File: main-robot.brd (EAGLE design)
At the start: 100 x 100 mm, 13 parts, among them U1 TEENSY_3.5_DIL

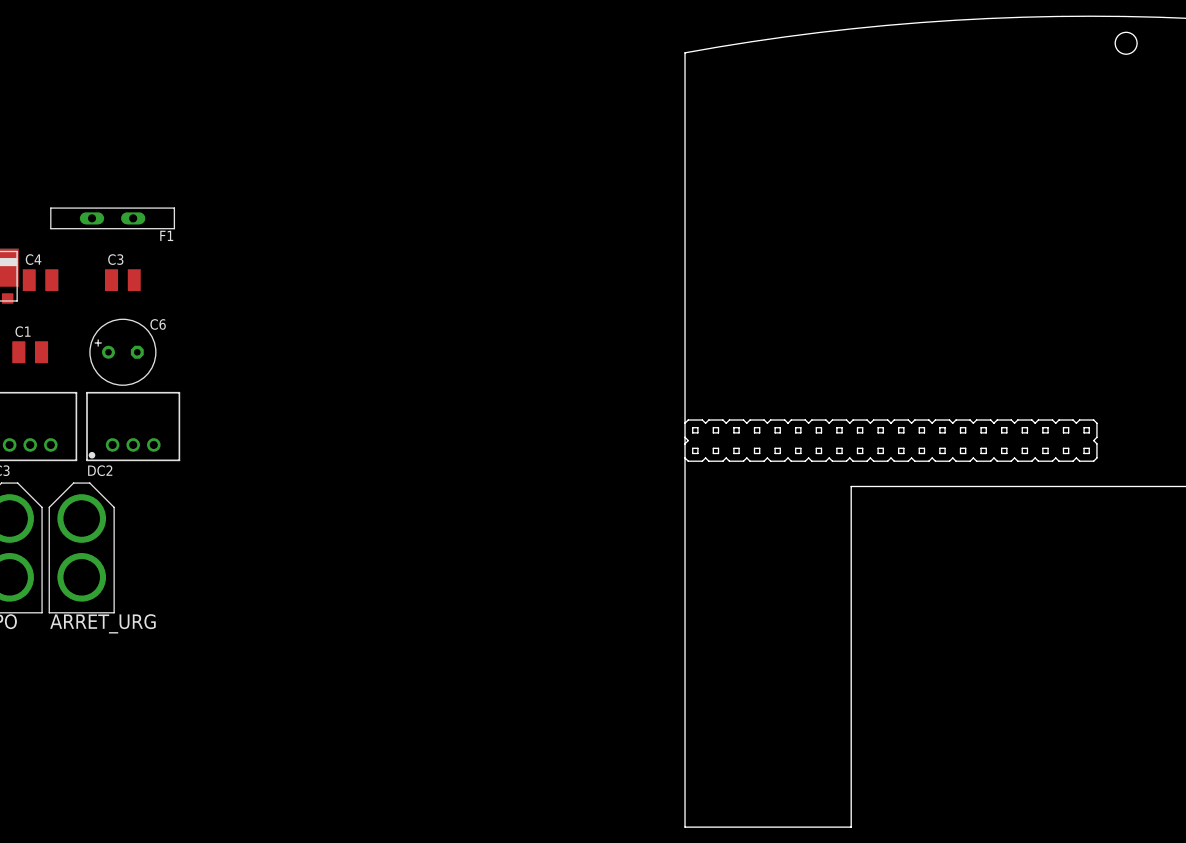
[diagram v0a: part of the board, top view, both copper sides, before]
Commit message: brd: rpi placement
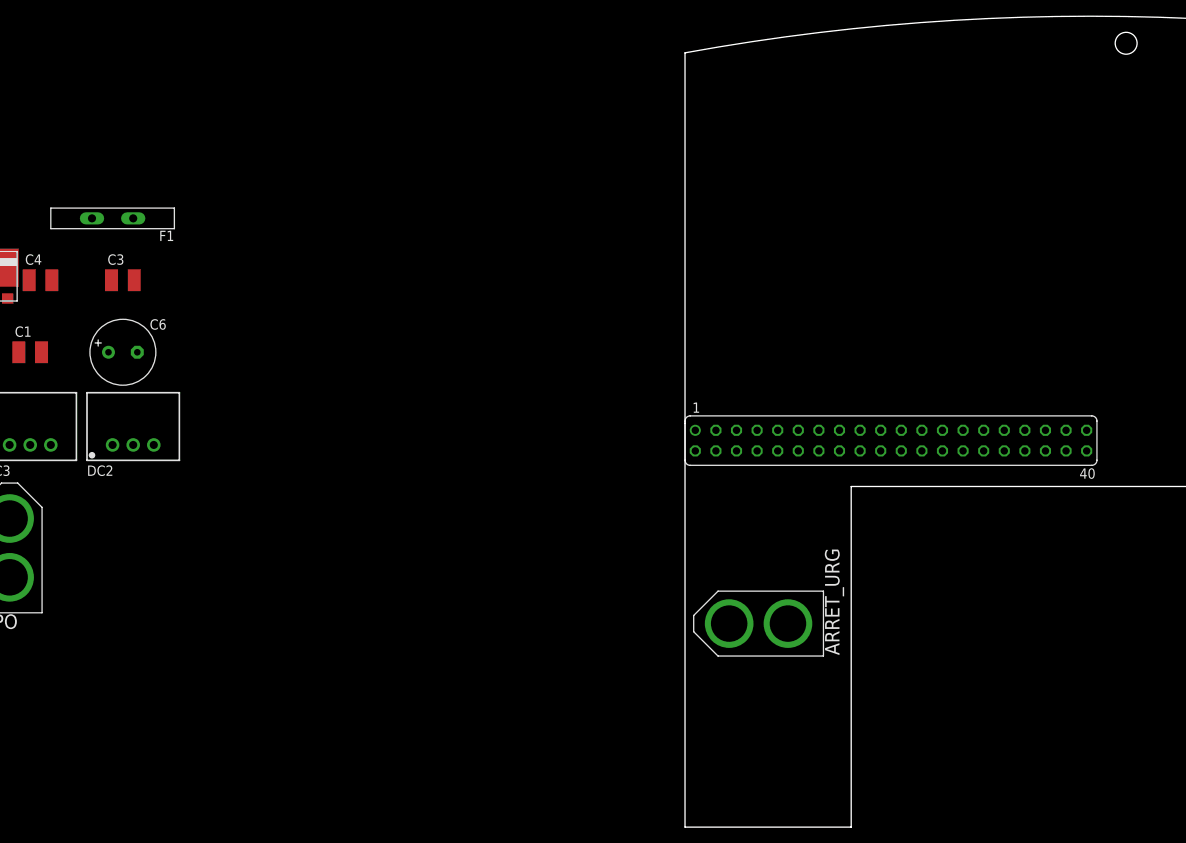
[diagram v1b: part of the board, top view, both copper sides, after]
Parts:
- added SV1: (no value), con-lsta:FE20-2
- moved ARRET_URG 84.0 mm to (9.07, 25.1), turned to 90 degrees
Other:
- outline, holes or cut-outs redrawn

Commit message: progess in schematic
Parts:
- removed ARRET_URG, LIPO: XT-60, con-xt:XT-60
- added AR-URG-1, AR-URG-2, LIPO+, LIPO-: TPPAD1-20Y, testpad:P1-20Y
- added C10, C8: 100nF, resistor:C0805
- added C7: 10nF, resistor:C0805
- added C9: 270µF, resistor:E3,5-8
- added CON1, CON2: AX12, con-molex-dynamixel:5267-03A
- added CON3: GENERIC-3PIN53253, con-molex-dynamixel:53253-0370
- added DISPLAY, ENC_D, ENC_G: JST-04TOP, con-jst-gh:BM04B-GHS
- added EXT_1: JST-06SIDE, con-jst-gh:SM06B-GHS
- added EXT_2: JST-06TOP, con-jst-gh:BM06B-GHS
- added JUMPER: JST-02SIDE, con-jst-gh:SM02B-GHS
- added LEVEL_SHIFTER1:Q1: BSS138, transistor-small-signal:SOT23
- added LEVEL_SHIFTER1:R1, LEVEL_SHIFTER1:R2, R5, R7: 10k, resistor:R0805
- added MOTOR: (no value), pinhead:1X06
- added R1, R2, R3, R4, R8: 1k, resistor:R0805
- added R6: 820, resistor:R0805
- added TOF_AR: JST-03SIDE, con-jst-gh:SM03B-GHS
- added TOF_ARD, TOF_ARG, TOF_AV: JST-03TOP, con-jst-gh:BM03B-GHS
- added U2: VNH7100AS, h-bridge:SOIC127P600X175-16M
- C1, C2, C3, C4: value 10µF/50V -> 10µF
- C5, C6: value 220µF/25V -> 220µF
- DC2: device dc-dc-converter:SIP3 -> traco-power:TSR1
- DC3: device dc-dc-converter:SIP3 -> traco-power:TSR2
- moved C5 132.5 mm to (36.0, 69.0)
- moved DC3 132.5 mm to (51.0, 61.0)
- moved DC2 121.8 mm to (51.0, 73.0)
- moved C6 108.5 mm to (37.0, 80.0)
- moved C4 108.4 mm to (27.0, 88.0)
- moved C3 108.3 mm to (37.0, 88.0)
- moved C2 108.1 mm to (15.0, 80.0)
- moved C1 107.9 mm to (25.0, 80.0)
- moved D1 98.5 mm to (3.00, 21.0)
- moved F1 95.9 mm to (1.70, 12.0), flipped to the bottom, turned to 270 degrees
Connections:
- removed net 3.3V: U1.3.3V, U1.3.3V3
- removed net AGND: U1.AGND
- removed net VIN: U1.VIN
- new net +12V: AR-URG-2.TP, C3.1, C4.1, C8.1, C9.+, CON1.2, CON2.2, DC2.1, EXT_1.5, EXT_2.5, U2.12, U2.4, U2.5
- new net +5V/1: C6.+, DC2.3, DISPLAY.4, ENC_D.4, ENC_G.4, MOTOR.4, U1.VIN
- new net +5V/2: C5.+, DC3.3, SV1.2, SV1.4
- new net 3V3: EXT_1.4, EXT_2.4, R7.1, TOF_AR.2, TOF_ARD.2, TOF_ARG.2, TOF_AV.2, U1.3.3V, U1.3.3V3
- new net AX12_DATA: CON1.1, CON2.1, EXT_1.2, EXT_2.2
- new net ENC_D_A: ENC_D.2
- new net ENC_D_B: ENC_D.1
- new net ENC_G_A: ENC_G.2
- new net ENC_G_B: ENC_G.1
- new net ENC_MOT_A: MOTOR.5
- new net ENC_MOT_B: MOTOR.6
- new net JUMPER: R8.1
- new net LEVEL_SHIFTER1:HV: LEVEL_SHIFTER1:R2.1
- new net LEVEL_SHIFTER1:IO_HV: LEVEL_SHIFTER1:Q1.3, LEVEL_SHIFTER1:R2.2
- new net LEVEL_SHIFTER1:IO_LV: LEVEL_SHIFTER1:Q1.2, LEVEL_SHIFTER1:R1.2
- new net LEVEL_SHIFTER1:LV: LEVEL_SHIFTER1:Q1.1, LEVEL_SHIFTER1:R1.1
- new net MOT_CS: C7.2, R5.1
- new net MOT_INA: R1.1
- new net MOT_INB: R2.1
- new net MOT_PWM: R3.1
- new net MOT_SEL: R4.1
- new net N$10: C10.2, JUMPER.1, R7.2, R8.2
- new net N$14: EXT_1.1
- new net N$15: EXT_2.1
- new net N$4: MOTOR.2, U2.10, U2.7
- new net N$5: R3.2, U2.11
- new net N$6: R2.2, U2.6
- new net N$7: R1.2, U2.3
- new net N$8: R4.2, U2.14
- new net N$9: R5.2, R6.2, U2.13
- new net SCL: DISPLAY.1
- new net SDA: DISPLAY.2
- new net TOF_DATA: EXT_1.3, EXT_2.3, TOF_AR.3, TOF_ARD.3, TOF_ARG.3, TOF_AV.3
- net GND: now also C10.1, C3.2, C4.2, C6.-, C7.1, C8.2, C9.-, CON1.3, CON2.3, DC2.2, DISPLAY.3, ENC_D.3, ENC_G.3, EXT_1.6, EXT_2.6, JUMPER.2, LIPO-.TP, MOTOR.3, R6.1, SV1.14, SV1.20, SV1.25, SV1.30, SV1.34, SV1.39, SV1.6, SV1.9, TOF_AR.1, TOF_ARD.1, TOF_ARG.1, TOF_AV.1, U1.AGND, U2.1, U2.16, U2.8, U2.9; no longer LIPO.(-)
- net N$1: now also AR-URG-1.TP
- net N$3: now also MOTOR.1, U2.15, U2.2; no longer C5.+, DC3.3
- net V_LIPO: now also LIPO+.TP; no longer LIPO.(+)
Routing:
- added copper zone on layer 1, net +12V

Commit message: progress on schematic
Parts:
- removed C2, C3: 10µF, resistor:C1210
- removed C7: 10nF, resistor:C0805
- removed LEVEL_SHIFTER1:Q1: BSS138, transistor-small-signal:SOT23
- removed LEVEL_SHIFTER1:R1, LEVEL_SHIFTER1:R2, R5: 10k, resistor:R0805
- removed R3, R4: 1k, resistor:R0805
- removed R6: 820, resistor:R0805
- removed U2: VNH7100AS, h-bridge:SOIC127P600X175-16M
- added D2: (no value), diode:SMB
- added DC1: TSR 1-2450, traco-power:TSR1
- added F2: MF-LSMF300, polyswitch:MF-LSMF300
- added HB1:C7, HB2:C7: 10nF, resistor:C0805
- added HB1:C8, HB2:C8: 100nF, resistor:C0805
- added HB1:C9, HB2:C9: 220µF, resistor:PANASONIC_D
- added HB1:R1, HB1:R2, HB1:R3, HB1:R4, HB1:R6, HB2:R1, HB2:R2, HB2:R3, HB2:R4, HB2:R6: 1k, resistor:R0805
- added HB1:R10, HB2:R10: 15k, resistor:R0805
- added HB1:R5, HB1:R9, HB2:R5, HB2:R9, S1:R1, S1:R2: 10k, resistor:R0805
- added HB1:U2, HB2:U2: VNH7100AS, h-bridge:SOIC127P600X175-16M
- added JMP1: 0R-JUMPA, jump-0r-smd:A0R-JMP
- added JP1: (no value), pinhead:1X02
- added LED1, LED2, LED3, LED4, LED5, LED6, LED7, LED8: (no value), led:1206
- added LEDS: JST-05SIDE, con-jst-gh:SM05B-GHS
- added S1:Q1: BSS138, transistor-small-signal:SOT23
- added SW1: SWITCH-SPDT-H, switch-rs-pro:SWITCH_SPDT_H
- added SW2, SW3, SW4, SW5, SW6, SW7: PUSH-BUTTON436331045822, push-button:436331045822
- C1, C4: value 10µF -> 22µF; device resistor:C1210 -> resistor:C0805
- C5, C6: device resistor:E3,5-8 -> resistor:PANASONIC_D
- C8: value 100nF -> 22µF
- C9: value 270µF -> 220µF; device resistor:E3,5-8 -> resistor:PANASONIC_D
- CON3: value GENERIC-3PIN53253 -> GENERIC-4PIN53253; device con-molex-dynamixel:53253-0370 -> con-molex-dynamixel:53253-0470
- R1, R2: value 1k -> 10k
- U1: value TEENSY_3.5_DIL -> TEENSY_3.5_DIL+4; device Teensy_libSG:TEENSY_3.5_DIL -> Teensy_libSG:TEENSY_3.5_DIL+4
- moved C10 134.8 mm to (-25.0, 60.0)
- moved R7 134.8 mm to (-25.0, 55.0)
- moved R8 134.8 mm to (-25.0, 50.0)
- moved C9 96.3 mm to (-101.0, -41.0)
- moved C8 92.7 mm to (-102.0, -49.0)
- moved R1 84.7 mm to (-94.0, -14.0)
- moved R2 84.7 mm to (-94.0, -19.0)
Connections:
- net N$14 renamed EXT_DATA
- removed net LEVEL_SHIFTER1:HV: LEVEL_SHIFTER1:R2.1
- removed net LEVEL_SHIFTER1:IO_HV: LEVEL_SHIFTER1:Q1.3, LEVEL_SHIFTER1:R2.2
- removed net LEVEL_SHIFTER1:IO_LV: LEVEL_SHIFTER1:Q1.2, LEVEL_SHIFTER1:R1.2
- removed net LEVEL_SHIFTER1:LV: LEVEL_SHIFTER1:Q1.1, LEVEL_SHIFTER1:R1.1
- removed net N$9: R5.2, R6.2, U2.13
- new net AREF: U1.AREF
- new net EXT_+5V: C9.+, DC1.3, HB2:C8.1, HB2:C9.+, HB2:U2.12, HB2:U2.4, HB2:U2.5, JMP1.1
- new net EXT_VCC: EXT_2.1, JMP1.2
- new net FLAG_CS: HB2:R10.2, HB2:R9.1
- new net FLAG_GPIO1: R1.1
- new net FLAG_GPIO2: R2.1
- new net FLAG_INA: HB2:R1.1
- new net FLAG_INB: HB2:R2.1
- new net FLAG_PWM: HB2:R3.1
- new net FLAG_SEL: HB2:R4.1
- new net HB1:N$13: HB1:C7.2, HB1:R5.1, HB1:R9.2
- new net HB1:N$5: HB1:R3.2, HB1:U2.11
- new net HB1:N$6: HB1:R2.2, HB1:U2.6
- new net HB1:N$7: HB1:R1.2, HB1:U2.3
- new net HB1:N$8: HB1:R4.2, HB1:U2.14
- new net HB1:N$9: HB1:R5.2, HB1:R6.2, HB1:U2.13
- new net HB2:N$13: HB2:C7.2, HB2:R5.1, HB2:R9.2
- new net HB2:N$5: HB2:R3.2, HB2:U2.11
- new net HB2:N$6: HB2:R2.2, HB2:U2.6
- new net HB2:N$7: HB2:R1.2, HB2:U2.3
- new net HB2:N$8: HB2:R4.2, HB2:U2.14
- new net HB2:N$9: HB2:R5.2, HB2:R6.2, HB2:U2.13
- new net LED_DATA: LEDS.5
- new net N$11: AR-URG-1.TP, D1.-, SW1.C
- new net N$12: D2.A, JP1.2
- new net S1:HV: S1:R2.1
- new net S1:IO_HV: S1:Q1.3, S1:R2.2
- new net S1:IO_LV: S1:Q1.2, S1:R1.2
- new net S1:LV: S1:Q1.1, S1:R1.1
- new net VUSB: JP1.1, U1.VUSB
- net +12V: now also DC1.1, F2.1, HB1:C8.1, HB1:C9.+, HB1:U2.12, HB1:U2.4, HB1:U2.5; no longer C3.1, C9.+, U2.12, U2.4, U2.5
- net +5V/1: now also D2.C, LEDS.3, LEDS.4
- net GND: now also DC1.2, HB1:C7.1, HB1:C8.2, HB1:C9.-, HB1:R10.1, HB1:R6.1, HB1:U2.1, HB1:U2.16, HB1:U2.8, HB1:U2.9, HB2:C7.1, HB2:C8.2, HB2:C9.-, HB2:R10.1, HB2:R6.1, HB2:U2.1, HB2:U2.16, HB2:U2.8, HB2:U2.9, LEDS.1, LEDS.2, SW1.CASE1, SW1.CASE2; no longer C2.2, C3.2, C7.1, R6.1, U2.1, U2.16, U2.8, U2.9
- net MOT_CS: now also HB1:R10.2, HB1:R9.1; no longer C7.2, R5.1
- net MOT_INA: now also HB1:R1.1; no longer R1.1
- net MOT_INB: now also HB1:R2.1; no longer R2.1
- net MOT_PWM: now also HB1:R3.1; no longer R3.1
- net MOT_SEL: now also HB1:R4.1; no longer R4.1
- net N$1: now also SW1.2; no longer AR-URG-1.TP, C2.1, D1.-
- net N$15: now also F2.2, JMP1.3; no longer EXT_2.1
- net N$3: now also HB1:U2.15, HB1:U2.2; no longer U2.15, U2.2
- net N$4: now also HB1:U2.10, HB1:U2.7; no longer U2.10, U2.7
- net N$5: now also CON3.1, HB2:U2.15, HB2:U2.2; no longer R3.2, U2.11
- net N$6: now also CON3.2, HB2:U2.10, HB2:U2.7; no longer R2.2, U2.6
- net N$7: now also CON3.3; no longer U2.3
- net N$8: now also CON3.4, R2.2; no longer R4.2, U2.14

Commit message: v1 schematics
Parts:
- removed CON3: GENERIC-4PIN53253, con-molex-dynamixel:53253-0470
- added FLAG: GENERIC-4PIN53253, con-molex-dynamixel:53253-0470
- added R10, R12, R14, R16, R4, R6, S2:R1, S2:R2, S3:R1, S3:R2, S4:R1, S4:R2, S5:R1, S5:R2: 10k, resistor:R0805
- added R11, R13, R15, R17, R18, R3, R5, R9: 470, resistor:R0805
- added RTC1: RTC, rtc-raspberry-pi:RTC
- added S2:Q1, S3:Q1, S4:Q1, S5:Q1: BSS138, transistor-small-signal:SOT23
- D2: value (none) -> SS56B
- JP1: value (none) -> VUSB
- SV1: value (none) -> RPI
- SW3, SW4: value PUSH-BUTTON436331045822 -> PUSH-BUTTON; device push-button:436331045822 -> push-button:PUSH-BUTTON
- U1: device Teensy_libSG:TEENSY_3.5_DIL+4 -> teensy:TEENSY_3.5_DIL+4
- moved LED7 252.5 mm to (-113.0, -248.0)
- moved SW7 221.8 mm to (47.7, 98.0)
- moved LED8 164.4 mm to (-113.0, -231.0)
- moved LED4 149.9 mm to (-113.0, -130.0)
- moved LED3 137.9 mm to (-113.0, -113.0)
- moved SW6 133.7 mm to (40.5, 97.9), turned to 2 degrees
- moved LED2 126.3 mm to (-115.0, -96.0)
- moved SW5 111.9 mm to (33.2, 97.5), turned to 3.5 degrees
- moved SW4 99.7 mm to (40.0, 85.0)
- moved SW3 74.1 mm to (28.0, 85.0), turned to 180 degrees
- moved SW2 54.5 mm to (25.8, 97.0), turned to 5.5 degrees
- moved C4 17.0 mm to (28.0, 71.0)
- moved C6 12.2 mm to (35.0, 68.0)
- moved C1 11.4 mm to (28.0, 69.0)
- moved LED5 10.0 mm to (-97.0, 4.00)
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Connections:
- removed net S1:HV: S1:R2.1
- removed net S1:IO_HV: S1:Q1.3, S1:R2.2
- removed net S1:IO_LV: S1:Q1.2, S1:R1.2
- removed net S1:LV: S1:Q1.1, S1:R1.1
- new net AX12_DATA_LV: S1:Q1.2, S1:R1.2, U1.10, U1.9
- new net EXT_DATA_LV: S2:Q1.2, S2:R1.2, U1.7, U1.8
- new net IN_COLOR_A: R16.1, SW7.2, SW7.4, U1.25
- new net IN_COLOR_B: R14.1, SW6.2, SW6.4, U1.26
- new net IN_JUMPER: C10.2, R7.2, R8.2, U1.6
- new net LED_COLOR_A: R15.2, U1.35/A16
- new net LED_COLOR_B: R13.2, U1.36/A17
- new net LED_DATA_LV: S5:Q1.2, S5:R1.2, U1.24
- new net LED_DEBUG_A: R17.2, U1.37/A18
- new net LED_DEBUG_B: R18.2, U1.38/A19
- new net N$13: RTC1.SDA, SV1.3
- new net N$14: RTC1.SCL, SV1.5
- new net N$16: LED2.A, R5.1
- new net N$17: LED3.A, R9.1
- new net N$18: LED4.A, R11.1
- new net N$19: LED7.A, R15.1
- new net N$20: LED5.A, R18.1
- new net N$21: LED6.A, R17.1
- new net N$9: LED1.A, R3.1
- new net RPI_3V3: R10.2, R12.2, R4.2, R6.2, RTC1.VIN, SV1.1
- new net RPI_IN_MATCH: R12.1, SV1.37, SW5.2, SW5.4
- new net RPI_IN_NET1: R6.1, SV1.11, SW3.3, SW3.4
- new net RPI_IN_NET2: R10.1, SV1.15, SW4.3, SW4.4
- new net RPI_IN_PWDN: R4.1, SV1.29, SW2.2, SW2.4
- new net RPI_LED_MATCH: R11.2, SV1.33
- new net RPI_LED_NET1: R5.2, SV1.13
- new net RPI_LED_NET2: R9.2, SV1.16
- new net RPI_LED_PWR: R3.2, SV1.31
- new net SCL_LV: S4:Q1.2, S4:R1.2, U1.19/A5
- new net SDA_LV: S3:Q1.2, S3:R1.2, U1.18/A4
- net +5V/1: now also S1:R2.1, S2:R2.1, S3:R2.1, S4:R2.1, S5:R2.1
- net 3V3: now also R14.2, R16.2, S1:Q1.1, S1:R1.1, S2:Q1.1, S2:R1.1, S3:Q1.1, S3:R1.1, S4:Q1.1, S4:R1.1, S5:Q1.1, S5:R1.1
- net AX12_DATA: now also S1:Q1.3, S1:R2.2
- net ENC_D_A: now also U1.11
- net ENC_D_B: now also U1.12
- net ENC_G_A: now also U1.34/A15
- net ENC_G_B: now also U1.33/A14
- net ENC_MOT_A: now also U1.14/A0
- net ENC_MOT_B: now also U1.15/A1
- net EXT_DATA: now also S2:Q1.3, S2:R2.2
- net FLAG_CS: now also U1.16/A2
- net FLAG_GPIO1: now also U1.31/A12
- net FLAG_GPIO2: now also U1.32/A13
- net FLAG_INA: now also U1.23/A9
- net FLAG_INB: now also U1.22/A8
- net FLAG_PWM: now also U1.21/A7
- net FLAG_SEL: now also U1.20/A6
- net GND: now also LED1.C, LED2.C, LED3.C, LED4.C, LED5.C, LED6.C, LED7.C, LED8.C, RTC1.GND, SW2.1, SW2.3, SW3.1, SW3.2, SW4.1, SW4.2, SW5.1, SW5.3, SW6.1, SW6.3, SW7.1, SW7.3
- net JUMPER: now also JUMPER.1
- net LED_DATA: now also S5:Q1.3, S5:R2.2
- net MOT_CS: now also U1.17/A3
- net MOT_INA: now also U1.2
- net MOT_INB: now also U1.3
- net MOT_PWM: now also U1.4
- net MOT_SEL: now also U1.5
- net N$10: now also LED8.A, R13.1; no longer C10.2, JUMPER.1, R7.2, R8.2
- net N$5: now also FLAG.1; no longer CON3.1
- net N$6: now also FLAG.2; no longer CON3.2
- net N$7: now also FLAG.3; no longer CON3.3
- net N$8: now also FLAG.4; no longer CON3.4
- net SCL: now also S4:Q1.3, S4:R2.2
- net SDA: now also S3:Q1.3, S3:R2.2
- net TOF_DATA: now also U1.0, U1.1

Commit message: brd: components placement
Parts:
- moved R15 382.8 mm to (47.0, 94.0), flipped to the bottom, turned to 180 degrees
- moved LED7 378.8 mm to (47.7, 95.0)
- moved R13 364.5 mm to (40.0, 94.0), flipped to the bottom, turned to 180 degrees
- moved R18 361.4 mm to (96.0, 24.0)
- moved LED8 360.3 mm to (40.6, 94.9), turned to 2 degrees
- moved R17 354.4 mm to (96.0, 22.0)
- moved R16 344.6 mm to (86.0, 29.0)
- moved S5:R2 331.1 mm to (80.0, 46.0), flipped to the bottom, turned to 270 degrees
- moved R14 329.5 mm to (86.0, 27.0)
- moved S5:R1 324.4 mm to (78.0, 46.0), flipped to the bottom, turned to 270 degrees
- moved S4:R2 318.7 mm to (80.0, 51.0), flipped to the bottom, turned to 270 degrees
- moved S5:Q1 315.6 mm to (75.0, 45.0), flipped to the bottom, turned to 270 degrees
- moved S4:R1 312.1 mm to (78.0, 51.0), flipped to the bottom, turned to 270 degrees
- moved S4:Q1 303.4 mm to (75.0, 50.0), flipped to the bottom, turned to 270 degrees
- moved S3:R2 291.8 mm to (69.0, 46.0), flipped to the bottom, turned to 270 degrees
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
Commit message: brd: begin routing
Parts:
- added C11, C2, C3, C7: 10µF, resistor:C0805
- moved F2 10.4 mm to (33.0, 69.0)
- moved JMP1 8.94 mm to (33.0, 75.0)
- moved HB1:C8 1.70 mm to (28.3, 53.0)
- moved LIPO+ 1.00 mm to (5.00, 2.50)
- moved LIPO- 1.00 mm to (15.5, 2.50)
- moved CON1 0.90 mm to (14.1, 40.0)
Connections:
- net +12V: now also C11.1, C2.1, C3.1, C7.1
- net GND: now also C11.2, C2.2, C3.2, C7.2
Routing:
- net +12V: track 0.00 -> 161.9 mm, vias 0 -> 1
- net EXT_VCC: track 0.00 -> 78.1 mm, vias 0 -> 2
- net +5V/2: track 0.00 -> 63.5 mm, vias 0 -> 1
- net N$11: track 0.00 -> 62.6 mm, vias 0 -> 2
- net EXT_+5V: track 0.00 -> 55.0 mm, vias 0 -> 1
- net N$1: track 0.00 -> 52.3 mm, vias 0 -> 1
- net N$3: track 0.00 -> 38.1 mm
- net N$4: track 0.00 -> 37.7 mm
- net GND: track 0.00 -> 20.2 mm
- net N$6: track 0.00 -> 13.9 mm
- net N$14: track 0.00 -> 10.7 mm
- net RPI_3V3: track 0.00 -> 10.7 mm
- net N$13: track 0.00 -> 10.7 mm
- net N$5: track 0.00 -> 10.3 mm
- net +5V/1: track 0.00 -> 7.13 mm
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- added copper zone on layer 1, net N$11
- added copper zone on layer 1, net N$2
- added copper zone on layer 1, net V_LIPO

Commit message: routing in progress
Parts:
- moved R2 73.9 mm to (65.6, 83.0), flipped to the bottom, turned to 90 degrees
- moved R1 71.4 mm to (67.7, 83.0), flipped to the bottom, turned to 90 degrees
- moved R17 66.3 mm to (94.3, 88.3), flipped to the bottom, turned to 270 degrees
- moved R18 64.3 mm to (96.4, 88.3), flipped to the bottom, turned to 270 degrees
- moved S2:R2 47.3 mm to (90.1, 8.70), turned to 180 degrees
- moved S2:Q1 46.7 mm to (90.1, 11.3), turned to 90 degrees
- moved S2:R1 43.7 mm to (90.1, 13.9), turned to 0 degrees
- moved S3:R2 33.9 mm to (69.4, 79.9), turned to 0 degrees
- moved S3:Q1 32.7 mm to (69.4, 77.3)
- moved S3:R1 28.8 mm to (69.4, 74.7), turned to 180 degrees
- moved S4:R2 28.6 mm to (73.6, 78.9), turned to 0 degrees
- moved S4:Q1 25.9 mm to (73.6, 75.9)
- moved HB2:R1 25.0 mm to (78.8, 92.0)
- moved S4:R1 22.7 mm to (73.6, 73.3), turned to 180 degrees
- moved S5:Q1 22.0 mm to (77.9, 66.8), turned to 180 degrees
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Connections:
- net FLAG_INA: now also U1.22/A8; no longer U1.23/A9
- net FLAG_INB: now also U1.21/A7; no longer U1.22/A8
- net FLAG_PWM: now also U1.20/A6; no longer U1.21/A7
- net FLAG_SEL: now also U1.23/A9; no longer U1.20/A6
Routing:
- net 3V3: track 0.00 -> 268.1 mm, vias 0 -> 7
- net AX12_DATA: track 0.00 -> 214.8 mm, vias 0 -> 2
- net TOF_DATA: track 0.00 -> 190.5 mm, vias 0 -> 4
- net +5V/1: track 7.13 -> 192.0 mm, vias 0 -> 6
- net LED_COLOR_B: track 0.00 -> 108.5 mm, vias 0 -> 1
- net LED_COLOR_A: track 0.00 -> 106.5 mm, vias 0 -> 1
- net IN_COLOR_B: track 0.00 -> 104.4 mm, vias 0 -> 2
- net IN_COLOR_A: track 0.00 -> 100.9 mm, vias 0 -> 2
- net +12V: track 161.9 -> 258.8 mm, vias 1 -> 3
- net FLAG_GPIO2: track 0.00 -> 88.0 mm, vias 0 -> 1
- net ENC_D_B: track 0.00 -> 86.6 mm, vias 0 -> 1
- net JUMPER: track 0.00 -> 86.2 mm, vias 0 -> 1
- net FLAG_GPIO1: track 0.00 -> 86.1 mm, vias 0 -> 1
- net ENC_D_A: track 0.00 -> 81.9 mm, vias 0 -> 1
- net LED_DATA: track 0.00 -> 78.6 mm, vias 0 -> 1
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
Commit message: routing v1
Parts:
- moved S1:Q1 3.59 mm to (74.6, 46.7)
- moved S1:R1 3.59 mm to (77.2, 46.7)
- moved S1:R2 3.59 mm to (72.0, 46.7)
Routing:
- net +5V/1: track 192.0 -> 264.2 mm, vias 6 -> 9
- net 3V3: track 268.1 -> 331.9 mm, vias 7 -> 10
- net ENC_MOT_B: track 64.2 -> 123.0 mm
- net ENC_MOT_A: track 61.0 -> 119.2 mm
- net TOF_DATA: track 190.5 -> 243.1 mm, vias 4 -> 8
- net AX12_DATA: track 214.8 -> 231.1 mm, vias 2 -> 4
- net ENC_D_A: track 81.9 -> 90.8 mm
- net ENC_D_B: track 86.6 -> 93.5 mm
- net LED_DATA_LV: track 59.6 -> 61.5 mm, vias 2 -> 4
- net AX12_DATA_LV: track 12.7 -> 11.8 mm
- net GND: vias 0 -> 17
- added copper zone on layer 1, net GND
- added copper zone on layer 16, net GND
